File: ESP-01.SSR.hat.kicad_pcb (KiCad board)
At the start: 2 copper layers, 12 parts, among them J1 Screw_Terminal_01x02, J2 Screw_Terminal_01x02, J3 Screw_Terminal_01x02, K1 G3MB-202P, K2 G3MB-202P, Q1 BC547, Q2 BC547, U1 ESP-01v090, U2 AMS1117-3.3

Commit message: updated wiring
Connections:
- K2 pad 1: Net-(J2-Pad2) -> Net-(J2-Pad1)
- K2 pad 2: Net-(J2-Pad1) -> Net-(J2-Pad2)
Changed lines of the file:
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@@
       (net 5 +5V))
     (pad 2 thru_hole circle (at 2.54 1.4) (size 1.508 1.508) (drill 1) (layers *.Cu *.Mask)
+      (net 4 "Net-(J2-Pad2)"))
+    (pad 1 thru_hole rect (at 10.16 1.4) (size 1.508 1.508) (drill 1) (layers *.Cu *.Mask)
       (net 3 "Net-(J2-Pad1)"))
-    (pad 1 thru_hole rect (at 10.16 1.4) (size 1.508 1.508) (drill 1) (layers *.Cu *.Mask)
-      (net 4 "Net-(J2-Pad2)"))
   )
   (module Package_TO_SOT_THT:TO-92_Inline (layer F.Cu)

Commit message: added tracks on pcb
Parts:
- J1, J2, J3: footprint TerminalBlock_TE-Connectivity:TerminalBlock_TE_282834-2_1x02_P2.54mm_Horizontal -> TerminalBlock:TerminalBlock_bornier-2_P5.08mm
- moved J1 4.62 mm to (142.2, 56.5)
- moved J2 2.29 mm to (142.2, 32.4)
- moved J3 1.80 mm to (142.2, 44.5)
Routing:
- net GND: track 0.00 -> 49.3 mm
- net +5V: track 0.00 -> 45.1 mm
- net Net-(Q2-Pad2): track 0.00 -> 25.8 mm
- net Net-(Q1-Pad2): track 0.00 -> 20.7 mm
- net Net-(J1-Pad2): track 0.00 -> 18.9 mm
- net Net-(J2-Pad2): track 0.00 -> 18.6 mm
- net +3.3V: track 0.00 -> 15.7 mm
- net Net-(J2-Pad1): track 0.00 -> 11.2 mm
- net Net-(J1-Pad1): track 0.00 -> 9.21 mm
- net Net-(R2-Pad2): track 0.00 -> 9.09 mm
- net Net-(J3-Pad2): track 0.00 -> 8.92 mm
- net Net-(J3-Pad1): track 0.00 -> 8.89 mm
- net Net-(R1-Pad1): track 0.00 -> 7.18 mm
- net Net-(K1-Pad4): track 0.00 -> 6.40 mm
- net Net-(K2-Pad4): track 0.00 -> 6.40 mm
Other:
- net class AC added: clearance 0.2, trace_width 2, via_dia 0.8, via_drill 0.4
- net class Default: trace_width 0.25 -> 0.5
- net class Power added: clearance 0.2, trace_width 1, via_dia 0.8, via_drill 0.4

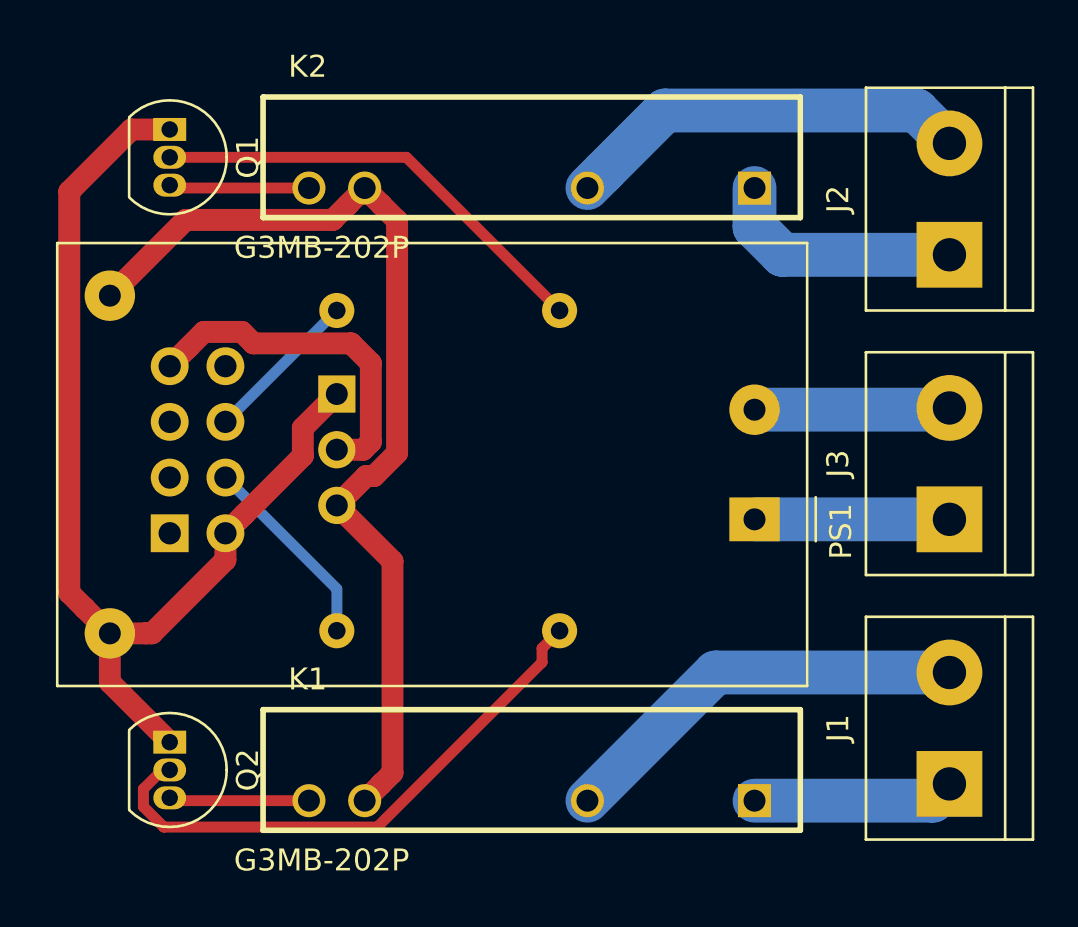
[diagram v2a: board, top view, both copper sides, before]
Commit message: added edge cuts
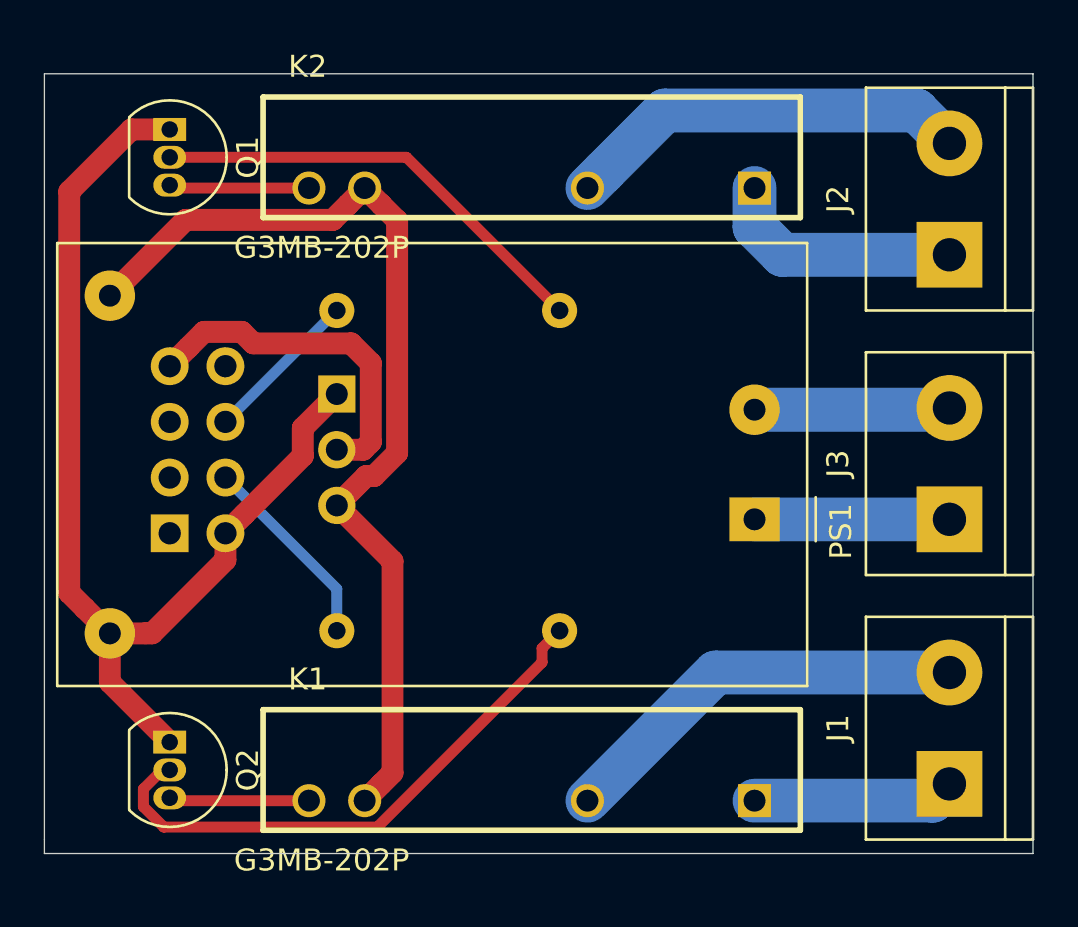
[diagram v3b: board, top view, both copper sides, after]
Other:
- board outline added: 45.1 x 35.6 mm
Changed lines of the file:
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@@
   (general
     (thickness 1.6)
-    (drawings 0)
+    (drawings 5)
     (tracks 70)
     (zones 0)
@@
     )
   )
+  (gr_line (start 146.05 59.69) (end 146.05 24.13) (layer Edge.Cuts) (width 0.05))
+  (gr_line (start 146.05 59.69) (end 100.965 59.69) (layer Edge.Cuts) (width 0.05))
+  (gr_line (start 100.965 59.055) (end 100.965 59.69) (layer Edge.Cuts) (width 0.05))
+  (gr_line (start 100.965 24.13) (end 100.965 59.055) (layer Edge.Cuts) (width 0.05))
+  (gr_line (start 146.05 24.13) (end 100.965 24.13) (layer Edge.Cuts) (width 0.05))
   (segment (start 131.575 51.435) (end 142.24 51.435) (width 2) (layer B.Cu) (net 1))
   (segment (start 125.73 57.28) (end 131.575 51.435) (width 2) (layer B.Cu) (net 1))
